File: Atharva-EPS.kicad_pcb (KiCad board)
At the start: 4 copper layers, 86.3 x 94.9 mm, 85 parts, among them J101 Conn_01x02_Female, J102 Conn_01x02_Female, J103 Conn_01x02_Female, J104 Conn_01x02_Female, J105 Conn_02x26_Odd_Even, J106 Conn_02x26_Odd_Even, J107 Conn_01x05_Female, J108 Conn_01x05_Female, J109 Conn_01x05_Female, J110 Conn_01x05_Female, J111 Conn_01x05_Female, J112 Conn_01x05_Female, Q101 P-MOSFET-SOT23-3, Q102 2N3906, Q103 2N3906, Q104 IRLML2060, Q105 IRLML2060, Q106 IRLML2060, Q107 IRLML2060, U101 MAX1615xUK, U102 MAX1615xUK, U103 S-8209AXXT, U104 S-8209AXXT, U107 LT3652EDD

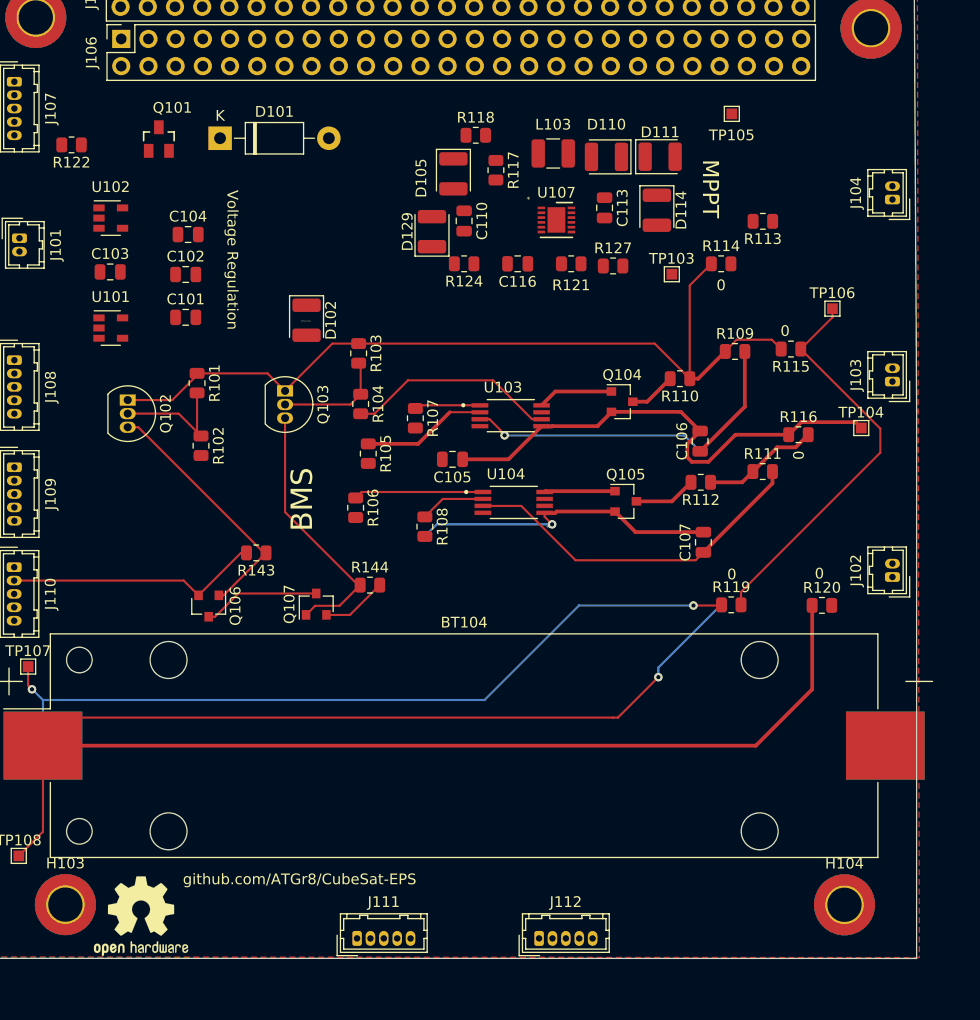
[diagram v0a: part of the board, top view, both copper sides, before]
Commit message: More manual routing
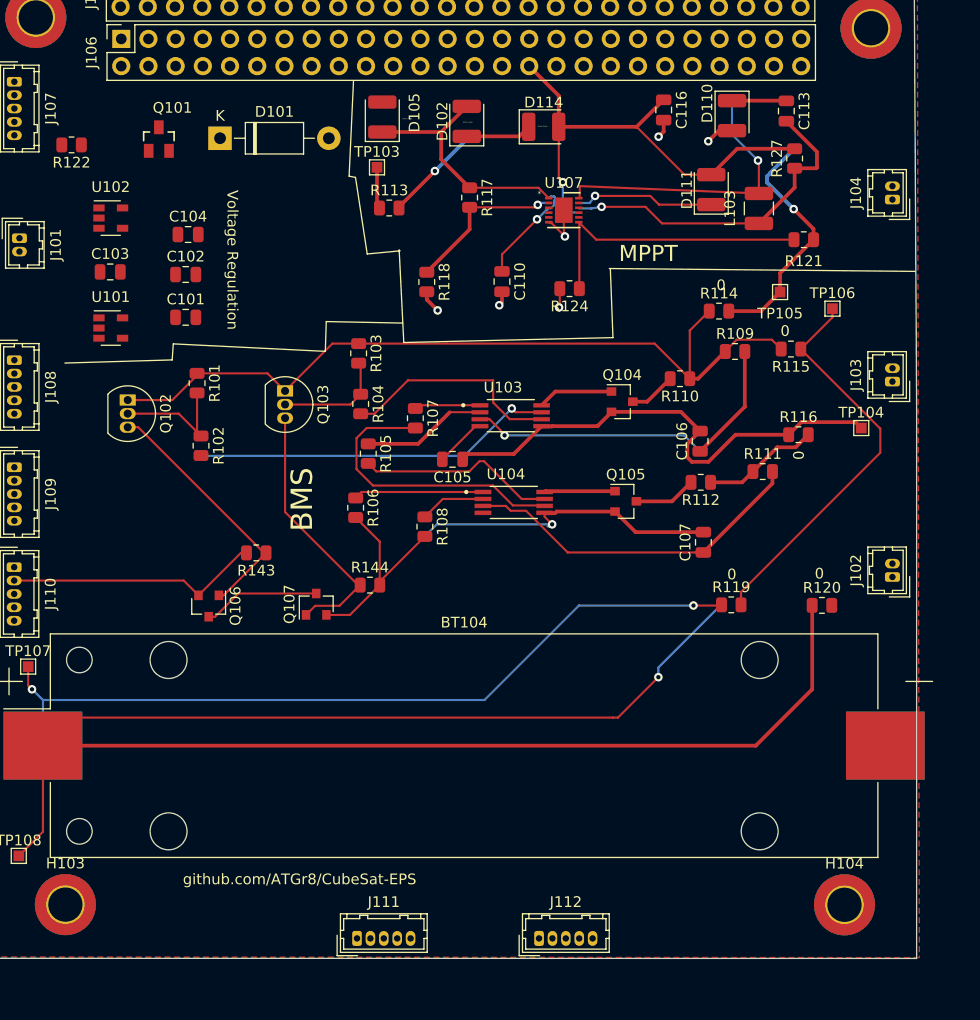
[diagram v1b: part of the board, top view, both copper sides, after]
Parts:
- removed D129: D, Diode_SMD:D_1210_3225Metric
- removed REF**: OSHW-Logo2_9.8x8mm_SilkScreen, Symbol:OSHW-Logo2_9.8x8mm_SilkScreen
- moved R113 34.9 mm to (127.0, 75.4), turned to 0 degrees
- moved TP103 29.3 mm to (125.8, 71.6)
- moved D102 23.8 mm to (134.2, 67.3), turned to 90 degrees
- moved R121 21.8 mm to (165.7, 78.4)
- moved L103 19.9 mm to (161.5, 75.5), turned to 270 degrees
- moved C116 19.8 mm to (152.6, 66.3), turned to 270 degrees
- moved R127 19.7 mm to (164.8, 70.8), turned to 90 degrees
- moved C113 19.2 mm to (164.1, 66.4)
- moved TP105 17.2 mm to (163.5, 83.3)
- moved R118 14.4 mm to (130.5, 82.3), turned to 270 degrees
- moved D114 13.1 mm to (141.4, 67.9), turned to 0 degrees
- moved D110 12.3 mm to (159.0, 66.8), turned to 270 degrees
- moved R124 10.1 mm to (143.8, 83.0)
- moved D105 8.50 mm to (126.3, 66.9), turned to 90 degrees
- moved C110 6.67 mm to (137.5, 82.3)
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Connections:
- C116 pad 1: MPPT_OUT -> Batt_in
- D102 pad 1: Net-(C102-Pad1) -> MPPT_OUT
- D102 pad 2: USB_Charge -> Net-(C110-Pad1)
- D111 pad 2: MPPT_OUT -> Batt_in
- D114 pad 1: Net-(C110-Pad1) -> MPPT_OUT
- D114 pad 2: MPPT_OUT -> Batt_in
- J106 pad 32: USB_Charge -> Batt_in
- R114 pad 2: USB_Charge -> Batt_in
- R121 pad 2: MPPT_OUT -> Batt_in
- R127 pad 2: MPPT_OUT -> Batt_in
- TP105 pad 1: USB_Charge -> Batt_in
- U107 pad 9: MPPT_OUT -> Batt_in
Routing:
- net Batt_in: track 0.00 -> 67.6 mm, vias 0 -> 2
- net Net-(R102-Pad2): track 0.00 -> 33.9 mm, vias 0 -> 1
- net Net-(C110-Pad1): track 0.00 -> 33.0 mm, vias 0 -> 1
- net Net-(C113-Pad1): track 0.00 -> 32.5 mm, vias 0 -> 1
- net Net-(C113-Pad2): track 0.00 -> 31.6 mm, vias 0 -> 1
- net Net-(R107-Pad2): track 0.00 -> 27.8 mm
- net Net-(R121-Pad1): track 0.00 -> 26.8 mm
- net Net-(R105-Pad2): track 0.00 -> 18.6 mm
- net MPPT_OUT: track 0.00 -> 15.8 mm, vias 0 -> 1
- net Net-(R117-Pad2): track 0.00 -> 15.3 mm, vias 0 -> 1
- net GND: track 23.9 -> 38.0 mm, vias 0 -> 6
- net B: track 36.1 -> 49.6 mm
- net Net-(D111-Pad1): track 0.00 -> 13.0 mm, vias 0 -> 1
- net Net-(C105-Pad2): track 0.00 -> 4.80 mm
- net Net-(Q102-Pad1): track 79.5 -> 75.0 mm
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
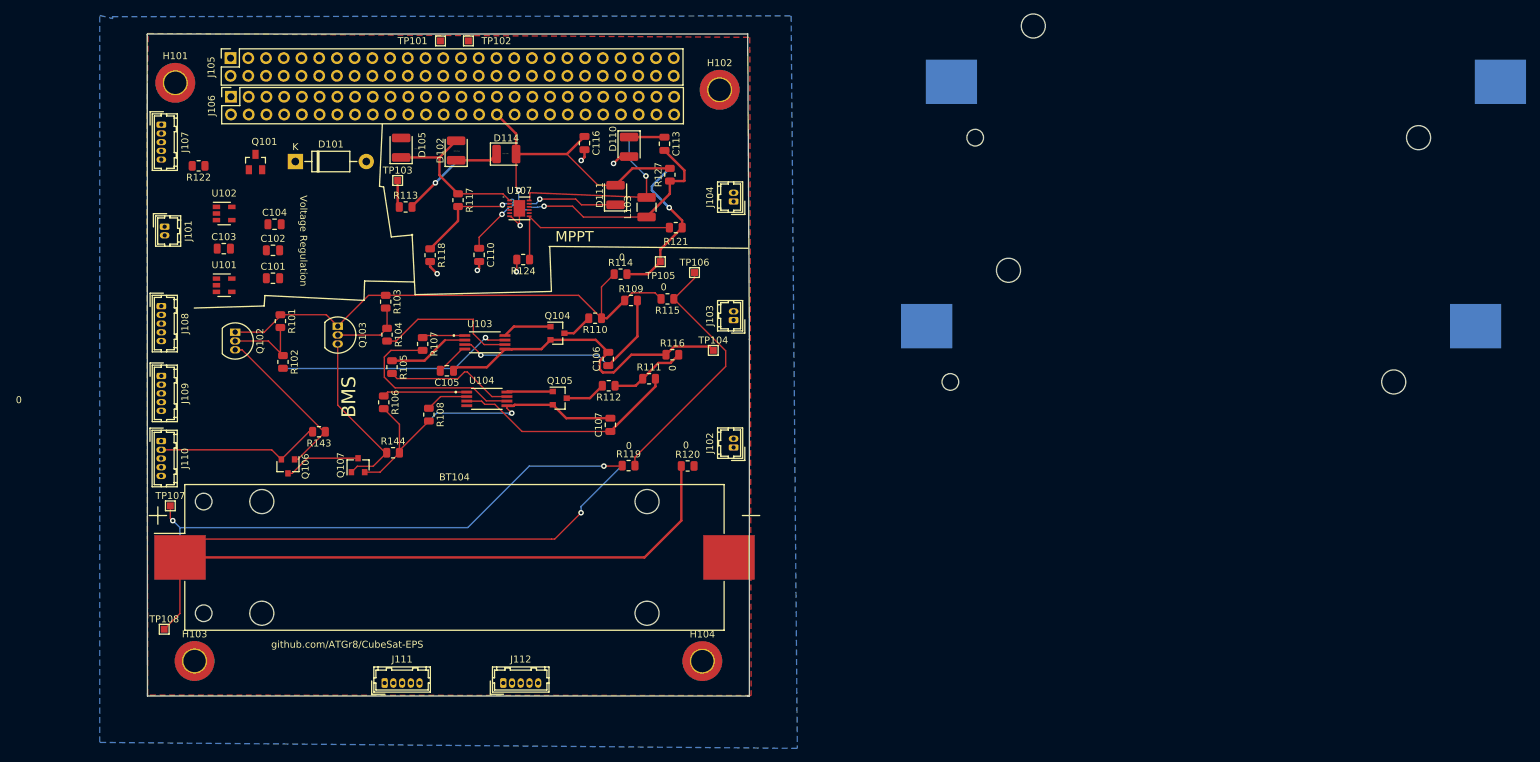
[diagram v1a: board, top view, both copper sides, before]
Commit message: Finished V1 pcb (just found out the voltage reg is wrong)
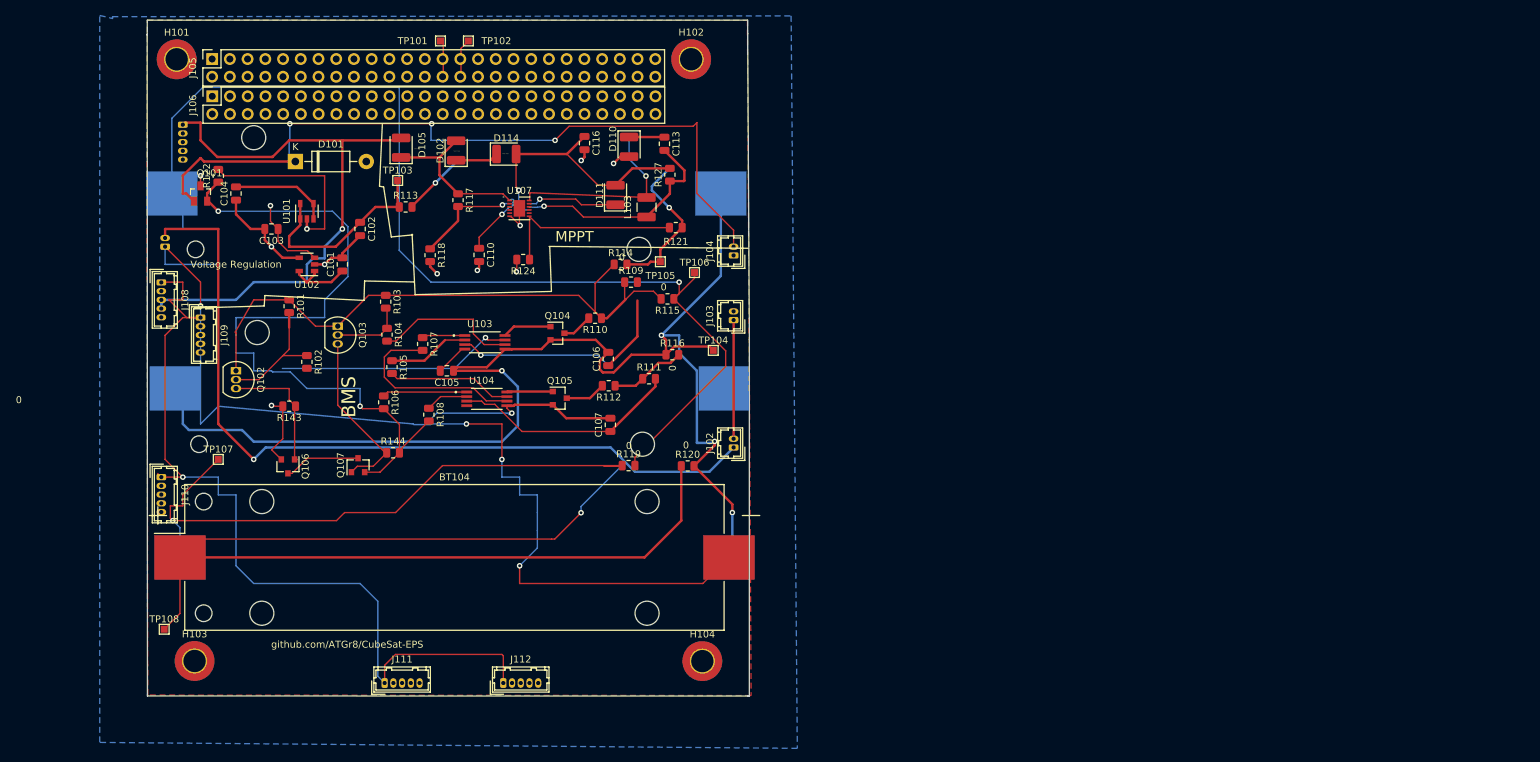
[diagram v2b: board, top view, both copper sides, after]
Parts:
- J101, J107: moved to B.Cu
- moved BT101 112.8 mm to (132.8, 73.5)
- moved BT102 108.0 mm to (133.3, 101.4)
- moved U101 15.9 mm to (112.8, 76.0), turned to 90 degrees
- moved U102 13.9 mm to (112.8, 83.7), turned to 180 degrees
- moved C102 12.8 mm to (120.5, 78.6), turned to -90 degrees
- moved C101 10.1 mm to (117.9, 83.7), turned to 90 degrees
- moved J109 10.1 mm to (97.6, 91.3)
- moved TP107 9.57 mm to (100.1, 111.6)
- moved Q101 9.07 mm to (97.6, 73.5)
- moved J104 7.73 mm to (174.0, 82.4)
- moved C103 7.39 mm to (107.8, 78.6), turned to 180 degrees
- moved C104 7.07 mm to (102.7, 73.5), turned to 90 degrees
- moved H102 5.99 mm to (167.9, 54.3)
- moved R143 5.62 mm to (110.3, 104.0)
- moved Q102 5.54 mm to (102.7, 98.9)
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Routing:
- net Solar_Out: track 0.00 -> 205.1 mm, vias 0 -> 2
- net A: track 0.00 -> 169.5 mm, vias 0 -> 5
- net Net-(BT101-Pad2): track 45.9 -> 185.8 mm, vias 0 -> 4
- net Net-(J101-Pad2): track 0.00 -> 116.4 mm, vias 0 -> 1
- net Net-(BT101-Pad1): track 37.5 -> 150.3 mm, vias 0 -> 1
- net Net-(D101-Pad1): track 0.00 -> 111.3 mm, vias 0 -> 3
- net B: track 49.6 -> 134.3 mm, vias 1 -> 3
- net GND: track 38.0 -> 75.1 mm, vias 6 -> 10
- net Net-(C102-Pad1): track 3.89 -> 28.9 mm
- net +5V: track 0.00 -> 19.5 mm
- net +3V3: track 0.00 -> 17.5 mm, vias 0 -> 1
- net Net-(J102-Pad2): track 0.00 -> 17.0 mm
- net Net-(BT103-Pad1): track 75.0 -> 88.8 mm, vias 2 -> 1
- net Net-(Q102-Pad1): track 75.0 -> 88.0 mm
- net Net-(C101-Pad1): track 0.00 -> 9.83 mm
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- removed copper zone on In1.Cu, net (none)
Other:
- board size 86.3 x 94.9 mm -> 86.3 x 96.9 mm
- copper layers 4 -> 2
- net class Default removed

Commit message: redesigned the board layout, traces and addded images
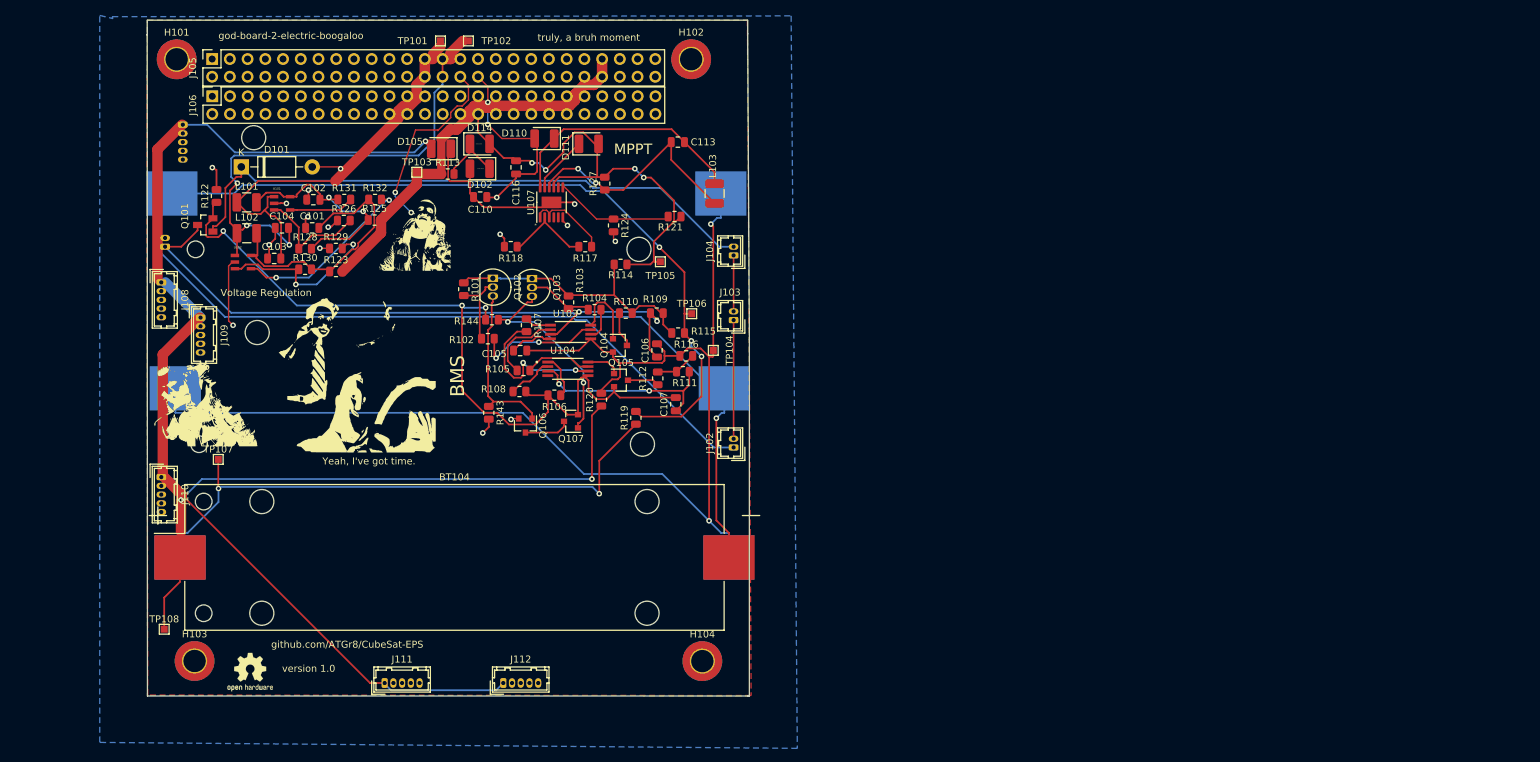
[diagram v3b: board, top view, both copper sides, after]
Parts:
- added G***: LOGO, time:timeFP, F.Cu at (122.0, 105.3)
- added G***: LOGO, drake1:drake1FP, F.Cu at (102.4, 105.3)
- added G***: LOGO, drake1:drake2FP, F.Cu at (133.2, 81.4)
- added G***: LOGO, Sunny:SunnyFP, F.Cu at (117.2, 94.6)
- added L101: L, Inductor_SMD:L_1210_3225Metric, F.Cu at (104.2, 74.8)
- added L102: L, Inductor_SMD:L_1210_3225Metric, F.Cu at (104.2, 79.2)
- added R123: 0, Resistor_SMD:R_0805_2012Metric, F.Cu at (117.0, 84.7)
- added R125: 0, Resistor_SMD:R_0805_2012Metric, F.Cu at (122.5, 77.3)
- added R126: 13.3k, Resistor_SMD:R_0805_2012Metric, F.Cu at (118.1, 77.4)
- added R128: 39.688k, Resistor_SMD:R_0805_2012Metric, F.Cu at (112.6, 81.4)
- added R129: 13.3k, Resistor_SMD:R_0805_2012Metric, F.Cu at (117.0, 81.4)
- added R130: 21.672k, Resistor_SMD:R_0805_2012Metric, F.Cu at (112.6, 84.4)
- added R131: 121k, Resistor_SMD:R_0805_2012Metric, F.Cu at (118.2, 74.4)
- added R132: 121k, Resistor_SMD:R_0805_2012Metric, F.Cu at (122.6, 74.4)
- added REF**: OSHW-Logo2_7.3x6mm_SilkScreen, Symbol:OSHW-Logo2_7.3x6mm_SilkScreen, F.Cu at (104.7, 142.1)
- C101, C102: value 0.1uF -> C
- C103, C104: value 6.8uF -> C
- U101, U102: value MAX1615xUK -> LT1930ES5TRMPBF; footprint Package_TO_SOT_SMD:SOT-23-5 -> LT1930ES5TRMPBF:SOT-5_S
- U107: value LT3652EDD -> LT3652EMSE; footprint Package_DFN_QFN:DFN-12-1EP_3x3mm_P0.45mm_EP1.66x2.38mm -> Package_SO:MSOP-12-1EP_3x4mm_P0.65mm_EP1.65x2.85mm
- moved Q102 39.1 mm to (139.5, 85.6)
- moved Q106 34.5 mm to (144.2, 106.8)
- moved Q107 31.2 mm to (150.7, 106.1), turned to 180 degrees
- moved R104 30.0 mm to (154.1, 90.1), turned to 0 degrees
- moved Q103 28.7 mm to (145.1, 85.7)
- moved R143 28.6 mm to (138.9, 104.9), turned to -90 degrees
- moved R103 26.2 mm to (150.3, 89.1)
- moved R102 26.1 mm to (138.8, 94.3), turned to 0 degrees
- moved R101 25.1 mm to (135.3, 87.2)
- moved R106 24.5 mm to (148.3, 102.4), turned to 180 degrees
- moved R144 23.8 mm to (139.4, 91.6), turned to 180 degrees
- moved R117 19.4 mm to (152.7, 81.1), turned to 180 degrees
- moved R105 18.9 mm to (143.9, 98.9), turned to 0 degrees
- moved R120 15.6 mm to (155.0, 103.0), turned to 90 degrees
- moved R107 15.1 mm to (144.3, 92.4)
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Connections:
- BT102 pad 2: A -> Net-(BT104-Pad1)
- BT104 pad 2: A -> Net-(BT104-Pad1)
- C101 pad 1: Net-(C101-Pad1) -> GND
- C101 pad 2: GND -> Net-(R123-Pad1)
- C102 pad 1: Net-(C102-Pad1) -> GND
- C102 pad 2: GND -> Net-(R125-Pad1)
- C103 pad 1: +3V3 -> GND
- C103 pad 2: GND -> +5V
- C104 pad 1: +5V -> GND
- C104 pad 2: GND -> +5V
- C110 pad 1: Net-(C110-Pad1) -> +BATT
- C110 pad 2: GND -> +BATT
- C116 pad 1: Batt_in -> +BATT
- C116 pad 2: GND -> +BATT
- D101 pad 2: GND -> +5V
- D102 pad 2: Net-(C110-Pad1) -> +BATT
- D105 pad 1: Net-(C110-Pad1) -> +BATT
- D105 pad 2: Solar_Out -> Net-(BT104-Pad1)
- D110 pad 2: GND -> +BATT
- D111 pad 2: Batt_in -> +BATT
- D114 pad 2: Batt_in -> +BATT
- J101 pad 1: A -> Net-(BT104-Pad1)
- J101 pad 2: Net-(J101-Pad2) -> Net-(BT104-Pad1)
- J102 pad 1: Net-(J101-Pad2) -> Net-(BT104-Pad1)
- J105 pad 1: Net-(J105-Pad1) -> unconnected-(J105-Pad1)
- J105 pad 10: Net-(J105-Pad10) -> unconnected-(J105-Pad10)
- J105 pad 11: Net-(J105-Pad11) -> unconnected-(J105-Pad11)
- J105 pad 12: Net-(J105-Pad12) -> unconnected-(J105-Pad12)
- J105 pad 13: Net-(J105-Pad13) -> unconnected-(J105-Pad13)
- J105 pad 14: Net-(J105-Pad14) -> unconnected-(J105-Pad14)
- J105 pad 15: Net-(J105-Pad15) -> unconnected-(J105-Pad15)
- J105 pad 16: Net-(J105-Pad16) -> unconnected-(J105-Pad16)
- J105 pad 17: Net-(J105-Pad17) -> unconnected-(J105-Pad17)
- J105 pad 18: Net-(J105-Pad18) -> unconnected-(J105-Pad18)
- J105 pad 19: Net-(J105-Pad19) -> unconnected-(J105-Pad19)
- J105 pad 2: Net-(J105-Pad2) -> unconnected-(J105-Pad2)
- J105 pad 20: Net-(J105-Pad20) -> unconnected-(J105-Pad20)
- J105 pad 21: Net-(J105-Pad21) -> unconnected-(J105-Pad21)
- J105 pad 22: Net-(J105-Pad22) -> unconnected-(J105-Pad22)
- J105 pad 23: Net-(J105-Pad23) -> unconnected-(J105-Pad23)
- J105 pad 24: Net-(J105-Pad24) -> unconnected-(J105-Pad24)
- J105 pad 27: +3V3 -> +5V
- J105 pad 28: +3V3 -> +5V
- J105 pad 29: GND -> +5V
- J105 pad 3: Net-(J105-Pad3) -> unconnected-(J105-Pad3)
- J105 pad 31: Net-(J105-Pad31) -> unconnected-(J105-Pad31)
- J105 pad 32: GND -> +BATT
- J105 pad 33: Net-(J105-Pad33) -> unconnected-(J105-Pad33)
- J105 pad 34: Net-(J105-Pad34) -> unconnected-(J105-Pad34)
- J105 pad 35: Net-(J105-Pad35) -> unconnected-(J105-Pad35)
- J105 pad 36: Net-(J105-Pad36) -> unconnected-(J105-Pad36)
- J105 pad 37: Net-(J105-Pad37) -> unconnected-(J105-Pad37)
- J105 pad 38: Net-(J105-Pad38) -> unconnected-(J105-Pad38)
- J105 pad 39: Net-(J105-Pad39) -> unconnected-(J105-Pad39)
- J105 pad 4: Net-(J105-Pad4) -> unconnected-(J105-Pad4)
- J105 pad 40: Net-(J105-Pad40) -> unconnected-(J105-Pad40)
- J105 pad 41: Net-(J105-Pad41) -> unconnected-(J105-Pad41)
- J105 pad 42: Net-(J105-Pad42) -> unconnected-(J105-Pad42)
- J105 pad 43: Net-(J105-Pad43) -> unconnected-(J105-Pad43)
- J105 pad 44: Net-(J105-Pad44) -> +BATT
- J105 pad 47: Net-(J105-Pad47) -> unconnected-(J105-Pad47)
- J105 pad 48: Net-(J105-Pad48) -> unconnected-(J105-Pad48)
- J105 pad 49: Net-(J105-Pad49) -> unconnected-(J105-Pad49)
- J105 pad 5: Net-(J105-Pad5) -> unconnected-(J105-Pad5)
- J105 pad 50: Net-(J105-Pad50) -> unconnected-(J105-Pad50)
- J105 pad 51: Net-(J105-Pad51) -> unconnected-(J105-Pad51)
- J105 pad 52: Net-(J105-Pad52) -> unconnected-(J105-Pad52)
- J105 pad 6: Net-(J105-Pad6) -> unconnected-(J105-Pad6)
- J105 pad 7: Net-(J105-Pad7) -> unconnected-(J105-Pad7)
- J105 pad 8: Net-(J105-Pad8) -> unconnected-(J105-Pad8)
- J105 pad 9: Net-(J105-Pad9) -> unconnected-(J105-Pad9)
- J106 pad 1: Net-(J106-Pad1) -> unconnected-(J106-Pad1)
- J106 pad 10: Net-(J106-Pad10) -> unconnected-(J106-Pad10)
- J106 pad 11: Net-(J106-Pad11) -> unconnected-(J106-Pad11)
- J106 pad 12: Net-(J106-Pad12) -> unconnected-(J106-Pad12)
- J106 pad 13: Net-(J106-Pad13) -> unconnected-(J106-Pad13)
- J106 pad 14: Net-(J106-Pad14) -> unconnected-(J106-Pad14)
- J106 pad 15: Net-(J106-Pad15) -> unconnected-(J106-Pad15)
- J106 pad 16: Net-(J106-Pad16) -> unconnected-(J106-Pad16)
- J106 pad 17: Net-(J106-Pad17) -> unconnected-(J106-Pad17)
- J106 pad 18: Net-(J106-Pad18) -> unconnected-(J106-Pad18)
- J106 pad 19: Net-(J106-Pad19) -> unconnected-(J106-Pad19)
- J106 pad 2: Net-(J106-Pad2) -> unconnected-(J106-Pad2)
- J106 pad 20: Net-(J106-Pad20) -> unconnected-(J106-Pad20)
- J106 pad 21: Net-(J106-Pad21) -> unconnected-(J106-Pad21)
- J106 pad 22: Net-(J106-Pad22) -> +5V
- J106 pad 23: Net-(J106-Pad23) -> +5V
- J106 pad 24: Net-(J106-Pad24) -> +5V
- J106 pad 25: Net-(J106-Pad25) -> +5V
- J106 pad 26: Net-(J106-Pad26) -> unconnected-(J106-Pad26)
- J106 pad 27: Net-(J106-Pad27) -> unconnected-(J106-Pad27)
- J106 pad 28: Net-(J106-Pad28) -> unconnected-(J106-Pad28)
- J106 pad 29: Net-(J106-Pad29) -> unconnected-(J106-Pad29)
- J106 pad 3: Net-(J106-Pad3) -> unconnected-(J106-Pad3)
- J106 pad 30: Net-(J106-Pad30) -> +BATT
- J106 pad 31: Net-(J106-Pad31) -> +BATT
- J106 pad 32: Batt_in -> +BATT
- J106 pad 33: Net-(J106-Pad33) -> +BATT
- J106 pad 34: Net-(J106-Pad34) -> +BATT
- J106 pad 35: Net-(J106-Pad35) -> +BATT
- J106 pad 36: Net-(J106-Pad36) -> +BATT
- J106 pad 37: Net-(J106-Pad37) -> +BATT
- J106 pad 38: Net-(J106-Pad38) -> +BATT
- J106 pad 39: Net-(J106-Pad39) -> +BATT
- J106 pad 4: Net-(J106-Pad4) -> unconnected-(J106-Pad4)
- J106 pad 40: Net-(J106-Pad40) -> +BATT
- J106 pad 41: I2C_DATA -> +BATT
- J106 pad 42: Net-(J106-Pad42) -> +BATT
- J106 pad 43: I2C_CLK -> +BATT
- J106 pad 44: Net-(J106-Pad44) -> unconnected-(J106-Pad44)
- J106 pad 45: Net-(J106-Pad45) -> unconnected-(J106-Pad45)
- J106 pad 46: Net-(J106-Pad46) -> unconnected-(J106-Pad46)
- J106 pad 47: Net-(J106-Pad47) -> unconnected-(J106-Pad47)
- J106 pad 48: Net-(J106-Pad48) -> unconnected-(J106-Pad48)
- J106 pad 49: Net-(J106-Pad49) -> unconnected-(J106-Pad49)
- J106 pad 5: Net-(J106-Pad5) -> unconnected-(J106-Pad5)
- J106 pad 50: Net-(J106-Pad50) -> unconnected-(J106-Pad50)
- J106 pad 51: Net-(J106-Pad51) -> unconnected-(J106-Pad51)
- J106 pad 52: Net-(J106-Pad52) -> unconnected-(J106-Pad52)
- J106 pad 6: Net-(J106-Pad6) -> unconnected-(J106-Pad6)
- J106 pad 7: Net-(J106-Pad7) -> unconnected-(J106-Pad7)
- J106 pad 8: Net-(J106-Pad8) -> unconnected-(J106-Pad8)
- J106 pad 9: Net-(J106-Pad9) -> unconnected-(J106-Pad9)
- J107 pad 1: Solar_Out -> Net-(BT104-Pad1)
- J107 pad 2: GND -> Net-(BT104-Pad1)
- J107 pad 3: Net-(J107-Pad3) -> unconnected-(J107-Pad3)
- J107 pad 4: Net-(J107-Pad4) -> unconnected-(J107-Pad4)
- J107 pad 5: Net-(J107-Pad5) -> unconnected-(J107-Pad5)
- J108 pad 1: Solar_Out -> Net-(BT104-Pad1)
- J108 pad 2: GND -> Net-(BT104-Pad1)
- J108 pad 3: Net-(J108-Pad3) -> unconnected-(J108-Pad3)
- J108 pad 4: Net-(J108-Pad4) -> unconnected-(J108-Pad4)
- J108 pad 5: Net-(J108-Pad5) -> unconnected-(J108-Pad5)
- J109 pad 1: Solar_Out -> Net-(BT104-Pad1)
- J109 pad 2: GND -> Net-(BT104-Pad1)
- J109 pad 3: Net-(J109-Pad3) -> unconnected-(J109-Pad3)
- J109 pad 4: Net-(J109-Pad4) -> unconnected-(J109-Pad4)
- J109 pad 5: Net-(J109-Pad5) -> unconnected-(J109-Pad5)
- J110 pad 1: Solar_Out -> Net-(BT104-Pad1)
- J110 pad 2: GND -> Net-(BT104-Pad1)
- J110 pad 3: Net-(J110-Pad3) -> unconnected-(J110-Pad3)
- J110 pad 4: Net-(J110-Pad4) -> unconnected-(J110-Pad4)
- J110 pad 5: Net-(J110-Pad5) -> unconnected-(J110-Pad5)
- J111 pad 1: Solar_Out -> Net-(BT104-Pad1)
- J111 pad 3: Net-(J111-Pad3) -> unconnected-(J111-Pad3)
- J111 pad 4: Net-(J111-Pad4) -> unconnected-(J111-Pad4)
- J111 pad 5: Net-(J111-Pad5) -> unconnected-(J111-Pad5)
- J112 pad 1: Solar_Out -> Net-(BT104-Pad1)
- J112 pad 3: Net-(J112-Pad3) -> unconnected-(J112-Pad3)
- J112 pad 4: Net-(J112-Pad4) -> unconnected-(J112-Pad4)
- J112 pad 5: Net-(J112-Pad5) -> unconnected-(J112-Pad5)
- Q101 pad 3: A -> Net-(BT104-Pad1)
- R113 pad 1: Net-(C102-Pad1) -> +BATT
- R114 pad 2: Batt_in -> +BATT
- R121 pad 2: Batt_in -> +BATT
- R127 pad 2: Batt_in -> +BATT
- TP102 pad 1: +3V3 -> +5V
- TP103 pad 1: Net-(C102-Pad1) -> +BATT
- TP105 pad 1: Batt_in -> +BATT
- U101 pad 1: Net-(C102-Pad1) -> +5V
- U101 pad 3: +5V -> Net-(R126-Pad2)
- U101 pad 4: +5V -> Net-(R131-Pad2)
- U101 pad 5: Net-(C102-Pad1) -> Net-(R125-Pad1)
- U102 pad 1: Net-(C101-Pad1) -> +5V
- U102 pad 3: +3V3 -> Net-(R129-Pad2)
- U102 pad 4: GND -> Net-(R132-Pad2)
- U102 pad 5: Net-(C101-Pad1) -> Net-(R123-Pad1)
- U104 pad 4: Net-(U104-Pad4) -> unconnected-(U104-Pad4)
- U107 pad 13: GND -> +BATT
- U107 pad 4: Net-(U107-Pad4) -> unconnected-(U107-Pad4)
- U107 pad 5: Net-(U107-Pad5) -> unconnected-(U107-Pad5)
- U107 pad 8: Net-(U107-Pad8) -> unconnected-(U107-Pad8)
- U107 pad 9: Batt_in -> +BATT
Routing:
- net Net-(BT104-Pad1): track 169.5 -> 468.2 mm, vias 1 -> 4
- net Solar_Out: track 205.1 -> 0.00 mm, vias 2 -> 0
- net +BATT: track 0.00 -> 182.1 mm, vias 0 -> 8
- net A: track 169.5 -> 0.00 mm, vias 5 -> 0
- net +5V: track 19.5 -> 137.7 mm, vias 0 -> 4
- net Net-(J101-Pad2): track 116.4 -> 0.00 mm, vias 1 -> 0
- net Batt_in: track 60.2 -> 0.00 mm, vias 2 -> 0
- net Net-(Q102-Pad1): track 88.0 -> 39.8 mm
- net Net-(R115-Pad1): track 150.3 -> 109.9 mm, vias 1 -> 3
- net Net-(R123-Pad1): track 0.00 -> 38.8 mm
- net Net-(R125-Pad1): track 0.00 -> 32.2 mm, vias 0 -> 2
- net Net-(C102-Pad1): track 28.9 -> 0.00 mm
- net Net-(R132-Pad2): track 0.00 -> 26.1 mm, vias 0 -> 2
- net Net-(R129-Pad2): track 0.00 -> 24.6 mm, vias 0 -> 2
- net Net-(D101-Pad1): track 111.3 -> 86.9 mm, vias 3 -> 0
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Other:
- board text added: "Yeah, I've got time."
- board text added: "god-board-2-electric-boogaloo"
- board text added: "truly, a bruh moment"
- board text added: "version 1.0"
- board text removed: "0"
